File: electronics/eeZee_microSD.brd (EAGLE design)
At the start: 30.4 x 18.3 mm, 13 parts, among them U1 MIC5317, U2 74HC4050, U4 MICROSD_CD

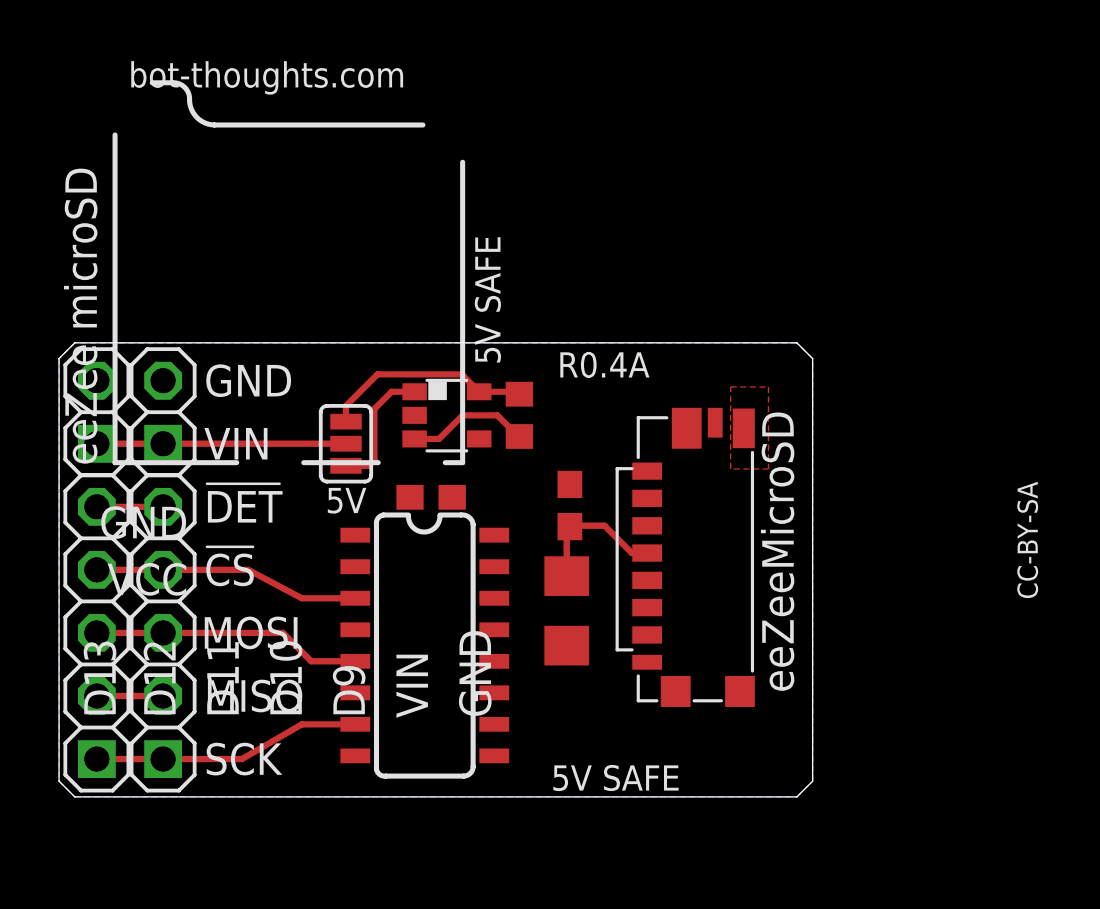
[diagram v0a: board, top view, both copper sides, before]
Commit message: finished routing, silk, added instructions and help url
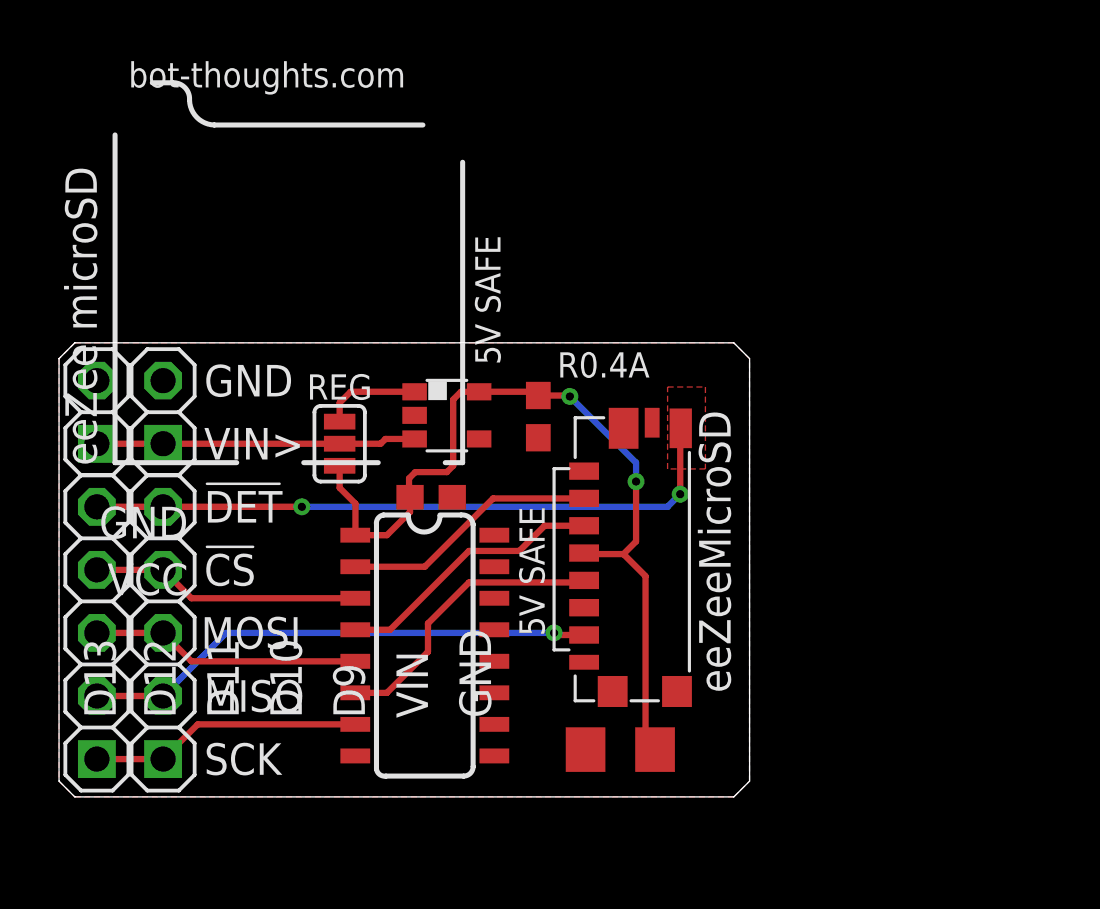
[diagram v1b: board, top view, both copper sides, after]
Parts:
- removed 5V: 3.3V, SparkFun:SJ_3
- removed R5: 10K, rcl:R0603
- added REG: SD, SparkFun:SJ_3
- moved U$5 12.4 mm to (22.2, 9.78)
- moved C1 5.99 mm to (22.6, 1.91), turned to 180 degrees
- moved C3 3.80 mm to (19.3, 15.3), turned to 270 degrees
- moved U4 2.54 mm to (19.9, 9.27)
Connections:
- removed net EN: R5.2, U1.3
- net VCC: now also REG.1; no longer 5V.1, R5.1
- net VIN: now also REG.2, U1.3; no longer 5V.2
- net VREGIN: now also REG.3; no longer 5V.3
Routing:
- net CD: track 2.67 -> 26.4 mm, vias 0 -> 2
- net VCC: track 14.1 -> 34.3 mm, vias 0 -> 2
- net MISO: track 2.67 -> 20.7 mm, vias 0 -> 1
- net SCK: track 0.00 -> 11.8 mm
- net MOSI: track 0.00 -> 11.0 mm
- net !SS: track 0.00 -> 10.4 mm
- net EN: track 4.97 -> 0.00 mm
- net VIN: track 10.0 -> 12.9 mm
- net VREGIN: track 5.19 -> 3.96 mm
- added copper zone on layer 1, net GND
- removed copper zone on layer 16, net GND
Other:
- board size 30.4 x 18.3 mm -> 27.8 x 18.3 mm
- board text added: "SOLDER JUMPER: IF VIN=3.3V, SOLDER SD IF VIN=5V, SOLDER REG https://goo.gl/NyRXp9"
- board text added: "VIN>"
- board text added: "cc-by-sa"

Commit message: fixed input/output caps per datasheet, changed DET to CD on silk
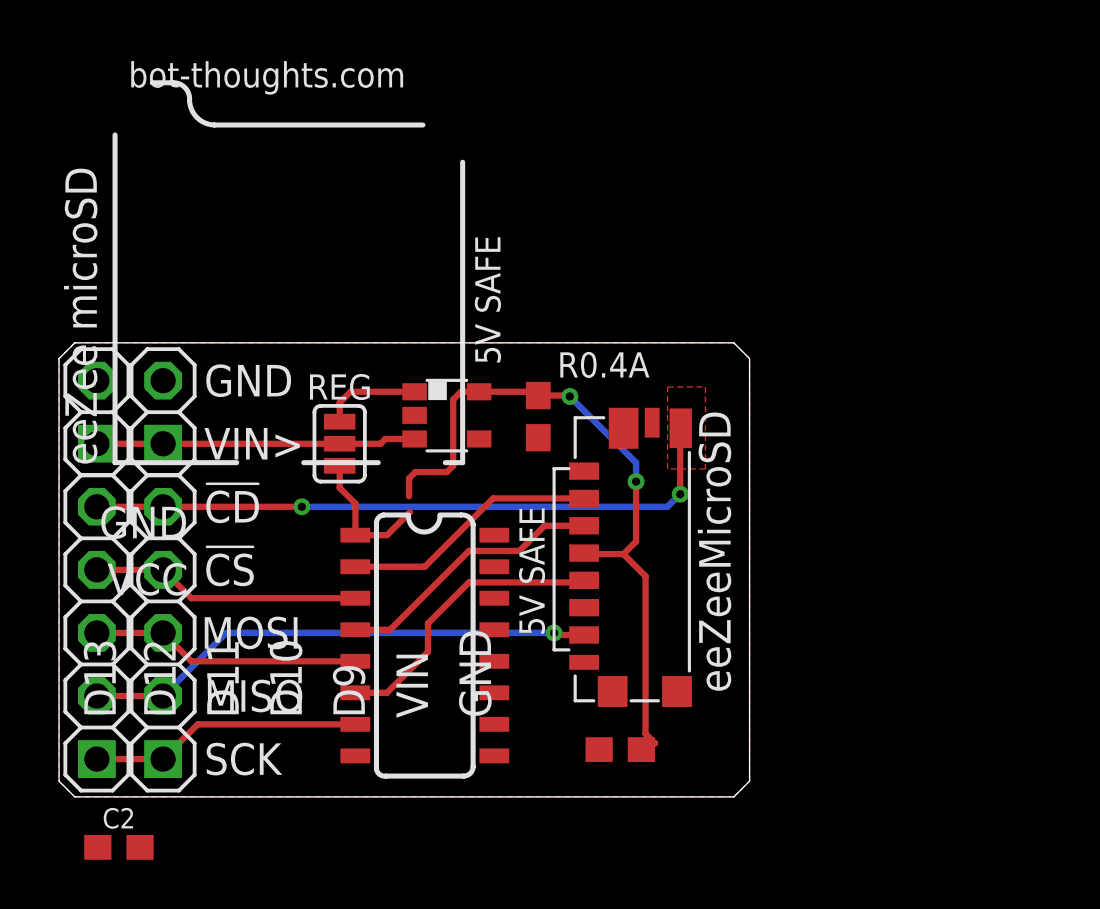
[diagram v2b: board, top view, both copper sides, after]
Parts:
- C1: value 106 -> 105; device rcl:C1206 -> bt_rcl:0603
- C2: value 104 -> 105; device rcl:C0603 -> bt_rcl:0603
- moved C2 18.9 mm to (2.41, -2.03)
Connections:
- net VCC: no longer C2.1
- net VREGIN: now also C2.1
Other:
- board text added: "!CD"
- board text removed: "!DET"
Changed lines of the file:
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@@
 <text x="15.3035" y="17.0815" size="0.8128" layer="122" font="vector" ratio="25" rot="MR90">MCP1824S</text>
 <text x="1.397" y="24.384" size="0.8128" layer="122" font="vector" ratio="25" rot="MR270">74HC4050</text>
-<text x="5.842" y="11.684" size="1.27" layer="25" font="vector" align="center-left">!DET</text>
+<text x="5.842" y="11.684" size="1.27" layer="25" font="vector" align="center-left">!CD</text>
 <text x="25.908" y="9.8806" size="1.27" layer="26" font="vector" rot="SMR90" align="bottom-center">eeZeeMicroSD</text>
 <text x="12.192" y="1.397" size="0.8128" layer="26" font="vector" ratio="10" rot="MR90">SOLDER JUMPER:
@@
 IF VIN=5V, SOLDER REG
 https://goo.gl/NyRXp9</text>
+<text x="5.588" y="9.144" size="1.27" layer="26" font="vector" rot="MR0" align="center-right">!CS</text>
+<text x="5.588" y="14.224" size="1.27" layer="26" font="vector" rot="MR0" align="center-right">VIN</text>
+<text x="5.588" y="16.764" size="1.27" layer="26" font="vector" rot="MR0" align="center-right">GND</text>
+<text x="5.715" y="6.604" size="1.27" layer="26" font="vector" rot="MR0" align="center-right">MOSI</text>
+<text x="5.588" y="4.064" size="1.27" layer="26" font="vector" rot="MR0" align="center-right">MISO</text>
+<text x="5.588" y="1.524" size="1.27" layer="26" font="vector" rot="MR0" align="center-right">SCK</text>
+<text x="5.588" y="11.684" size="1.27" layer="26" font="vector" rot="MR0" align="center-right">!CD</text>
 </plain>
 <attributes>
@@
 <attribute name="VALUE" x="13.5255" y="17.0815" size="0.8128" layer="27" font="vector" ratio="10"/>
 </element>
-<element name="C1" library="rcl" package="C1206" value="106" x="22.606" y="1.905" smashed="yes" rot="R180">
+<element name="C1" library="bt_rcl" package="0603" value="105" x="22.606" y="1.905" smashed="yes" rot="R180">
 <attribute name="PARTNO" value="LMK107B7105KA-T" x="22.606" y="1.905" size="1.778" layer="27" rot="R180" display="off"/>
 <attribute name="VALUE" x="19.939" y="0.889" size="0.8128" layer="27" font="vector" ratio="12" rot="R90"/>
@@
 <element name="U2" library="SparkFun" package="SO016" value="74HC4050" x="14.732" y="6.096" smashed="yes" rot="R270">
 <attribute name="VALUE" x="14.351" y="8.509" size="0.8128" layer="27" font="vector" ratio="10" rot="R270"/>
-</element>
-<element name="C2" library="rcl" package="C0603" value="104" x="14.986" y="12.065" smashed="yes">
-<attribute name="PARTNO" value="LMK107B7105KA-T" x="14.986" y="12.065" size="1.778" layer="27" display="off"/>
-<attribute name="DATABASE" value="./../../../eagle/PARTSDB.TXT" x="14.986" y="12.065" size="1.778" layer="27" display="off"/>
-<attribute name="VALUE" x="13.97" y="12.7" size="0.8128" layer="27" font="vector" ratio="10"/>
 </element>
 <element name="C3" library="rcl" package="C0603" value="104" x="19.304" y="15.3162" smashed="yes" rot="R270">
@@
 <element name="U4" library="bt_electromech" package="USD_SMALL" value="MICROSD_CD" x="19.939" y="9.271" smashed="yes" rot="R90"/>
 <element name="U$5" library="bt" package="BTLOGOS" value="BTLOGO-LOGO-SM" x="22.225" y="9.779" rot="MR90"/>
+<element name="C2" library="bt_rcl" package="0603" value="105" x="2.413" y="-2.032">
+<attribute name="PARTNO" value="LMK107B7105KA-T" x="2.413" y="-2.032" size="0.8128" layer="27" font="vector" ratio="10" display="off"/>
+</element>
 </elements>
 <signals>
@@
 <contactref element="U1" pad="2"/>
 <contactref element="C1" pad="2"/>
-<contactref element="C2" pad="2"/>
 <contactref element="JP1" pad="2"/>
 <contactref element="C3" pad="2"/>
@@
 <contactref element="U4" pad="GND3"/>
 <contactref element="U4" pad="GND4"/>
+<contactref element="C2" pad="2"/>
+<wire x1="11.932" y1="1.651" x2="3.263" y2="-2.032" width="0" layer="19" extent="1-1"/>
 </signal>
 <signal name="MOSI_HV">
@@
 <wire x1="11.745" y1="16.317" x2="11.303" y2="15.875" width="0.254" layer="1"/>
 <wire x1="11.303" y1="15.875" x2="11.303" y2="15.113" width="0.254" layer="1"/>
+<contactref element="C2" pad="1"/>
+<wire x1="1.563" y1="-2.032" x2="11.303" y2="15.113" width="0" layer="19" extent="1-1"/>
 </signal>
 <signal name="!CS_HV">
@@
 <contactref element="C1" pad="1"/>
 <contactref element="REG" pad="1"/>
-<contactref element="C2" pad="1"/>
 <contactref element="U2" pad="1"/>
 <contactref element="C3" pad="1"/>
@@
 <wire x1="11.938" y1="11.811" x2="11.938" y2="10.547" width="0.254" layer="1"/>
 <wire x1="11.938" y1="10.547" x2="11.932" y2="10.541" width="0.254" layer="1"/>
-<wire x1="14.136" y1="12.065" x2="14.136" y2="11.469" width="0.254" layer="1"/>
 <wire x1="14.136" y1="11.469" x2="13.208" y2="10.541" width="0.254" layer="1"/>
 <wire x1="13.208" y1="10.541" x2="11.932" y2="10.541" width="0.254" layer="1"/>
@@
 <wire x1="14.351" y1="13.081" x2="14.097" y2="12.827" width="0.254" layer="1"/>
 <wire x1="14.097" y1="12.827" x2="14.097" y2="12.104" width="0.254" layer="1"/>
-<wire x1="14.097" y1="12.104" x2="14.136" y2="12.065" width="0.254" layer="1"/>
 <wire x1="19.304" y1="16.1662" x2="20.5368" y2="16.1662" width="0.254" layer="1"/>
 <wire x1="20.5368" y1="16.1662" x2="20.574" y2="16.129" width="0.254" layer="1"/>
@@
 <wire x1="22.733" y1="9.779" x2="21.191" y2="9.779" width="0.254" layer="1"/>
 <wire x1="21.191" y1="9.779" x2="21.149" y2="9.821" width="0.254" layer="1"/>
-<wire x1="24.006" y1="1.905" x2="24.006" y2="2.156" width="0.254" layer="1"/>
+<wire x1="23.456" y1="1.905" x2="24.006" y2="2.156" width="0.254" layer="1"/>
 <wire x1="24.006" y1="2.156" x2="23.622" y2="2.54" width="0.254" layer="1"/>
 <wire x1="23.622" y1="2.54" x2="23.622" y2="8.89" width="0.254" layer="1"/>
 <wire x1="23.622" y1="8.89" x2="22.733" y2="9.779" width="0.254" layer="1"/>
+<wire x1="14.136" y1="11.469" x2="14.097" y2="12.104" width="0" layer="19" extent="1-1"/>
 </signal>
 <signal name="VIN">

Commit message: moved solder jumper to bottom, tweaked silk, changed board layout.
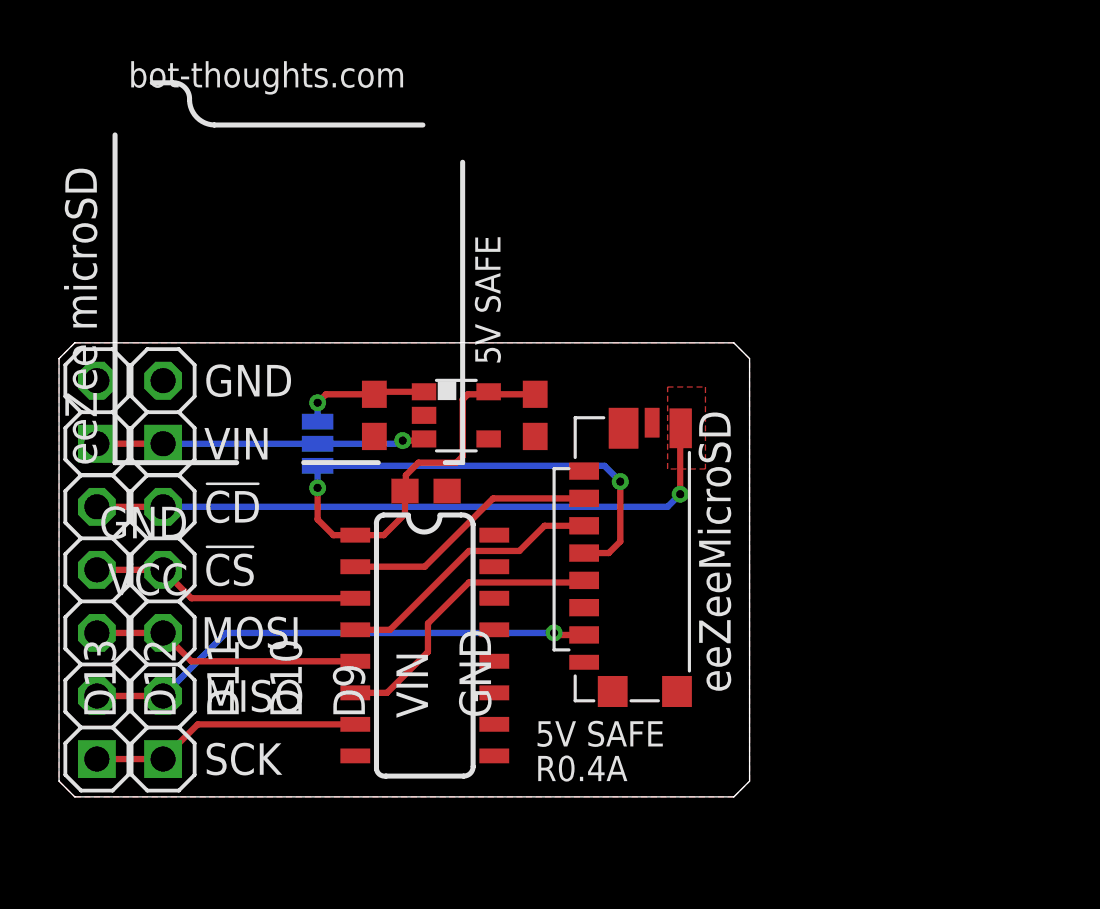
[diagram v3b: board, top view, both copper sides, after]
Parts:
- moved C2 20.2 mm to (12.7, 15.4), turned to 270 degrees
- moved C1 13.9 mm to (19.2, 15.4), turned to 270 degrees
- moved C3 5.42 mm to (14.8, 12.3), turned to 0 degrees
- moved REG 0.89 mm to (10.4, 14.2), flipped to the bottom
- moved U1 0.38 mm to (16.0, 15.4)
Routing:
- net VCC: track 34.0 -> 32.4 mm
- net VREGIN: track 3.96 -> 5.23 mm, vias 0 -> 1
- net VIN: track 12.9 -> 13.3 mm, vias 0 -> 1
- net CD: vias 2 -> 1
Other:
- board text removed: "VIN>"

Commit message: changed layout, silk, reg/byp, pwr routing, sd package (centered)
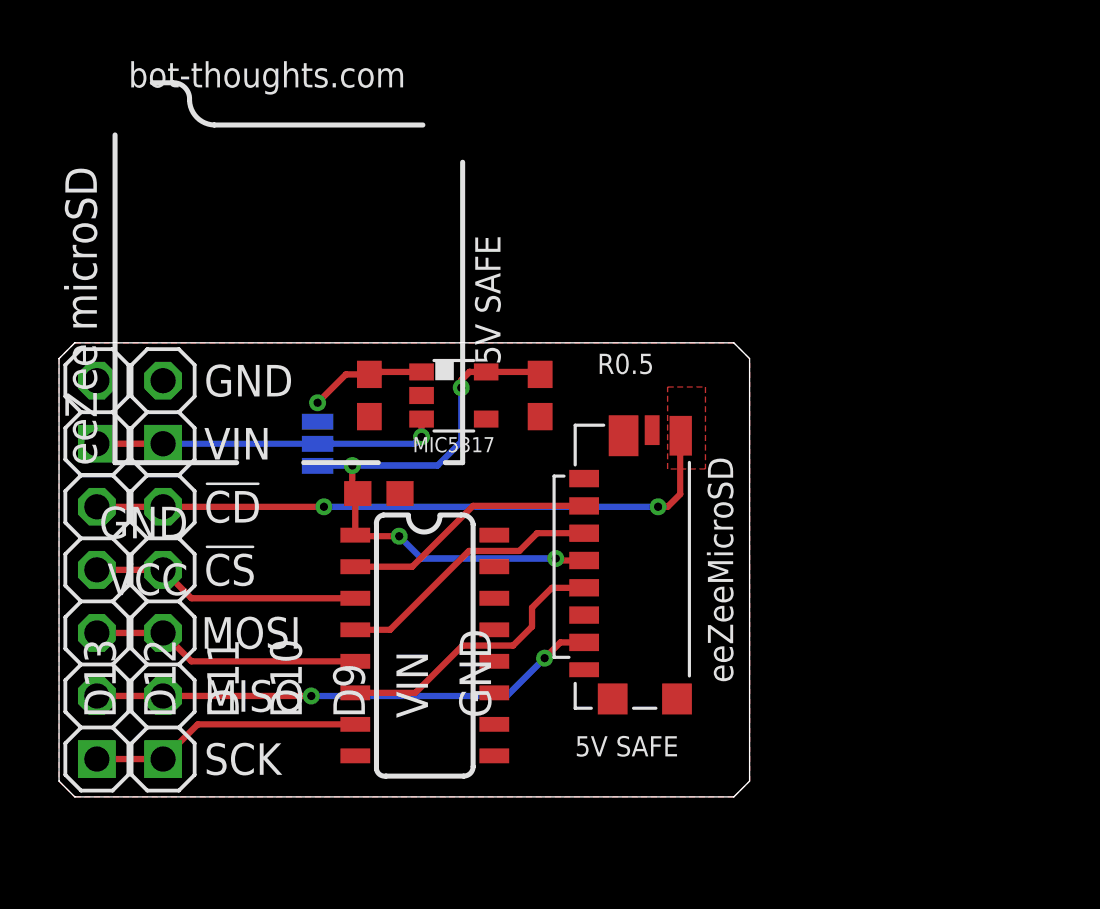
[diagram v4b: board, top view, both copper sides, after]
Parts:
- REG/BYP: value SD -> (none)
- moved C3 1.90 mm to (12.9, 12.2)
- moved C1 0.82 mm to (19.4, 16.2)
- moved C2 0.82 mm to (12.5, 16.2)
- moved U1 0.81 mm to (15.9, 16.2)
- moved U$5 0.63 mm to (22.2, 9.14)
- renumbered REG to REG/BYP
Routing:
- net VCC: track 32.4 -> 24.6 mm, vias 2 -> 4
- net VIN: track 13.3 -> 13.9 mm
- net VREGIN: track 5.23 -> 4.67 mm
- net CD: track 26.4 -> 26.6 mm, vias 1 -> 2
- net MISO: track 20.7 -> 20.5 mm, vias 1 -> 2
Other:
- board text added: "R0.5"
- board text removed: "R0.4A"
